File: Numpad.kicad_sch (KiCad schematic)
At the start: 196 parts, among them J1 USB_C_Receptacle_USB2.0, J2 USB_C_Receptacle_USB2.0, J3 AVR-ISP-6, Q1 DMN2041L, Q2 DMN2041L, SW1 SW_Push, SW10 SW_Push, SW11 SW_Push, SW12 SW_Push, SW13 SW_Push, SW14 SW_Push, SW15 SW_Push, SW17 SW_Push, SW18 SW_Push, SW2 SW_Push, SW20 SW_Push, SW21 SW_Push, SW23 SW_Push, SW24 SW_Push, SW25 SW_Push, SW27 SW_Push, SW28 SW_Push, SW3 SW_Push, SW30 SW_Push, SW31 SW_Push, SW32 SW_Push, SW33 SW_Push, SW34 SW_Push, SW35 SW_Push, SW36 SW_Push, SW37 SW_Push, SW38 SW_Push, SW39 SW_Push, SW4 SW_Push, SW40 SW_Push, SW41 SW_Push, SW42 SW_Push, SW43 SW_Push, SW44 SW_Push, SW45 SW_Push, SW46 SW_Push, SW47 SW_Push, SW5 SW_Push, SW6 SW_Push, SW7 SW_Push, SW8 SW_Push, SW9 SW_Push, U1 ATmega32U4-A, Y1 16MHz

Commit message: added a numpad
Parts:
- removed D10, D12, D13, D15, D22, D24, D25, D37, D4, D43, D49, D58, D66, D71, D77, D80, D81, D84, D89: D_Small, symbol Device:D_Small
- removed D11, D14, D18, D20, D26, D3, D31, D35, D39, D40, D61, D63, D67, D7, D73, D76, D79, D8, D82: LED, symbol Device:LED
- removed D?: PRTR5V0U2X, Package_TO_SOT_SMD:SOT-143, symbol Power_Protection:PRTR5V0U2X
- removed J2: USB_C_Receptacle_USB2.0, symbol Connector:USB_C_Receptacle_USB2.0
- removed R10: 1k, symbol Device:R_Small
- removed R11, R12, R13, R14, R17, R19, R25, R28, R36, R40, R42, R43, R45, R48, R50, R53, R54, R8: 470, symbol Device:R_Small
- removed R16, R26: 4.7K, symbol Device:R_Small
- removed R32, R51: 5.1k, symbol Device:R_Small
- removed SW1, SW13, SW2, SW21, SW23, SW25, SW3, SW30, SW31, SW36, SW37, SW4, SW40, SW41, SW42, SW45, SW7, SW8, SW9: SW_Push, keyswitches.pretty-2:Kailh_socket_PG1350, symbol Switch:SW_Push
- added D? (x2): D_Small, symbol Device:D_Small
- added D? (x2): LED, symbol Device:LED
- added R? (x2): 470, symbol Device:R_Small
- added SW? (x2): SW_Push, keyswitches.pretty-2:Kailh_socket_PG1350, symbol Switch:SW_Push
- R6: value 470 -> 1k
- renumbered SW28 to SW_RESET1
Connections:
- net +5V: now also D?.2 (A), D?.2 (A)
- net COL_0: now also SW?.2
- net COL_1: now also SW?.2
- net ROW_3: now also D?.1 (K)
- net ROW_4: now also D?.1 (K)
- net at D1.1 (K): now also R3.1
- net at Q1.3 (D), R1.2, R15.2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: now also R?.2, R?.2; no longer R3.2, R6.2
- net at R6.1: now also Q2.1 (G)
- net at Q2.3 (D): now also R3.2
- net CAPS_LOCK_PWM renamed NUM_LOCK_PWM
- net NUM_LOCK_PWM: now also R6.2
- net COL_5: no longer names the net of U1.36 (PF7)
- net ROW_5: no longer names the net of U1.29 (PB5)
- net ROW_6: no longer names the net of U1.30 (PB6)
- new net: D?.2 (A), SW?.1 (x2)
- new net: D?.1 (K), R?.1 (x2)
- no-connect marks 10 -> 13
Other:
- note added: "24 LEDs"
- note added: "24 switch matrix"
- note added: "NUM LOCK LED"
- note added: "NUMPAD"
- note removed: "41 LEDs"
- note removed: "41 switch matrix"
- note removed: "CAPS LOCK LED"
- note removed: "RIGHT KEEEB HALF"
- note removed: "USB-C Left HALF"
- moved on the sheet: D17, D19, D2, D21, D33, D34, D44, D46, D48, D50, D52, D56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

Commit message: numpad pcb start
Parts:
- removed D27, D28, D41, D57, D70: D_Small, symbol Device:D_Small
- removed D48, D91, D? (x2): LED, symbol Device:LED
- removed R35, R52, R? (x2): 470, symbol Device:R_Small
- removed SW10, SW11, SW14, SW17, SW33: SW_Push, keyswitches.pretty-2:Kailh_socket_PG1350, symbol Switch:SW_Push
- added D2: D_Small, Diode_SMD:D_SOD-123, symbol Device:D_Small
- added SW2: SW_Push, keyswitches.pretty-2:Kailh_socket_PG1350, symbol Switch:SW_Push
- C1, C2, C3, C4, C5, C6, C7: footprint (none) -> Capacitor_SMD:C_0402_1005Metric
- D10: renamed from D78; footprint (none) -> Diode_SMD:D_SOD-123
- D101: renamed from D83; footprint (none) -> LED_SMD:LED_PLCC_2835
- D102: renamed from D2; footprint (none) -> LED_SMD:LED_PLCC_2835
- D103: renamed from D9; footprint (none) -> LED_SMD:LED_PLCC_2835
- D104: renamed from D62; footprint (none) -> LED_SMD:LED_PLCC_2835
- D105: renamed from D74; footprint (none) -> LED_SMD:LED_PLCC_2835
- D106: renamed from D46; footprint (none) -> LED_SMD:LED_PLCC_2835
- D107: renamed from D17; footprint (none) -> LED_SMD:LED_PLCC_2835
- D108: renamed from D19; footprint (none) -> LED_SMD:LED_PLCC_2835
- D109: renamed from D56; footprint (none) -> LED_SMD:LED_PLCC_2835
- D11: renamed from D42; footprint (none) -> Diode_SMD:D_SOD-123
- D110: renamed from D44; footprint (none) -> LED_SMD:LED_PLCC_2835
- D111: renamed from D52; footprint (none) -> LED_SMD:LED_PLCC_2835
- D112: renamed from D88; footprint (none) -> LED_SMD:LED_PLCC_2835
- D113: renamed from D33; footprint (none) -> LED_SMD:LED_PLCC_2835
- D114: renamed from D75; footprint (none) -> LED_SMD:LED_PLCC_2835
- D115: renamed from D34; footprint (none) -> LED_SMD:LED_PLCC_2835
- D116: renamed from D72; footprint (none) -> LED_SMD:LED_PLCC_2835
- D117: renamed from D50; footprint (none) -> LED_SMD:LED_PLCC_2835
- D118: renamed from D64; footprint (none) -> LED_SMD:LED_PLCC_2835
- D119: renamed from D85; footprint (none) -> LED_SMD:LED_PLCC_2835
- D12: renamed from D87; footprint (none) -> Diode_SMD:D_SOD-123
- D120: renamed from D86; footprint (none) -> LED_SMD:LED_PLCC_2835
- D125: renamed from D1; footprint (none) -> LED_SMD:LED_PLCC_2835
- D13: renamed from D30; footprint (none) -> Diode_SMD:D_SOD-123
- D14: renamed from D16; footprint (none) -> Diode_SMD:D_SOD-123
- D15: renamed from D5; footprint (none) -> Diode_SMD:D_SOD-123
- D16: renamed from D51; footprint (none) -> Diode_SMD:D_SOD-123
- D17: renamed from D47; footprint (none) -> Diode_SMD:D_SOD-123
- D18: renamed from D6; footprint (none) -> Diode_SMD:D_SOD-123
- D19: renamed from D29; footprint (none) -> Diode_SMD:D_SOD-123
- D20: renamed from D45; footprint (none) -> Diode_SMD:D_SOD-123
- D21: renamed from D68; footprint (none) -> Diode_SMD:D_SOD-123
- D3, D7: renamed from D?; footprint (none) -> Diode_SMD:D_SOD-123
- D4: renamed from D60; footprint (none) -> Diode_SMD:D_SOD-123
- D5: renamed from D54; footprint (none) -> Diode_SMD:D_SOD-123
- D6: renamed from D23; footprint (none) -> Diode_SMD:D_SOD-123
- D8: renamed from D69; footprint (none) -> Diode_SMD:D_SOD-123
- D9: renamed from D90; footprint (none) -> Diode_SMD:D_SOD-123
- F1: footprint (none) -> Keebio-Parts:Fuse_0805
- J1: footprint (none) -> Connector_USB:USB_C_Receptacle_HRO_TYPE-C-31-M-12
- J3: footprint (none) -> Keebio-Parts:ICSP_1.27mm
- R101: renamed from R30; footprint (none) -> Resistor_SMD:R_0402_1005Metric
- R102: renamed from R39; footprint (none) -> Resistor_SMD:R_0402_1005Metric
- R103: renamed from R5; footprint (none) -> Resistor_SMD:R_0402_1005Metric
- R104: renamed from R1; footprint (none) -> Resistor_SMD:R_0402_1005Metric
- R105: renamed from R37; footprint (none) -> Resistor_SMD:R_0402_1005Metric
- R106: renamed from R46; footprint (none) -> Resistor_SMD:R_0402_1005Metric
- R107: renamed from R47; footprint (none) -> Resistor_SMD:R_0402_1005Metric
- R108: renamed from R18; footprint (none) -> Resistor_SMD:R_0402_1005Metric
- R109: renamed from R49; footprint (none) -> Resistor_SMD:R_0402_1005Metric
- R110: renamed from R7; footprint (none) -> Resistor_SMD:R_0402_1005Metric
- R111: renamed from R24; footprint (none) -> Resistor_SMD:R_0402_1005Metric
- R112: renamed from R33; footprint (none) -> Resistor_SMD:R_0402_1005Metric
- R113: renamed from R38; footprint (none) -> Resistor_SMD:R_0402_1005Metric
- R114: renamed from R29; footprint (none) -> Resistor_SMD:R_0402_1005Metric
- R115: renamed from R9; footprint (none) -> Resistor_SMD:R_0402_1005Metric
- R116: renamed from R20; footprint (none) -> Resistor_SMD:R_0402_1005Metric
- R117: renamed from R27; footprint (none) -> Resistor_SMD:R_0402_1005Metric
- R118: renamed from R15; footprint (none) -> Resistor_SMD:R_0402_1005Metric
- R119: renamed from R4; footprint (none) -> Resistor_SMD:R_0402_1005Metric
- R120: renamed from R41; footprint (none) -> Resistor_SMD:R_0402_1005Metric
- R121: renamed from R21; footprint (none) -> Resistor_SMD:R_0402_1005Metric
- R2, R22, R23, R3, R31, R34, R44, R6: footprint (none) -> Resistor_SMD:R_0402_1005Metric
- U1: footprint ATmega32U4:ATmega32U4 -> Package_QFP:TQFP-44_10x10mm_P0.8mm
- Y1: footprint (none) -> Crystal:Crystal_SMD_3225-4Pin_3.2x2.5mm
- gave numbers to parts that had none: 2
- renumbered D21 to D1, Q1 to Q101, SW39 to SW10, SW44 to SW11, SW5 to SW12, SW47 to SW13, SW20 to SW14, SW18 to SW15, SW27 to SW16, SW32 to SW17, SW24 to SW18, SW12 to SW19, SW38 to SW20, SW35 to SW21, SW34 to SW4, SW6 to SW5, SW15 to SW6, SW43 to SW8, SW46 to SW9
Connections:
- net COL_0: now also SW2.2
- net ROW_4: now also D2.1 (K)
- net COL_4: no longer names the net of U1.37 (PF6)
- new net: D2.2 (A), SW2.1
- no-connect marks 13 -> 14
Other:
- note added: "20 LEDs"
- note added: "20 SWITCH MATRIX"
- note removed: "24 LEDs"
- note removed: "24 switch matrix"
- moved on the sheet: Q101, R121

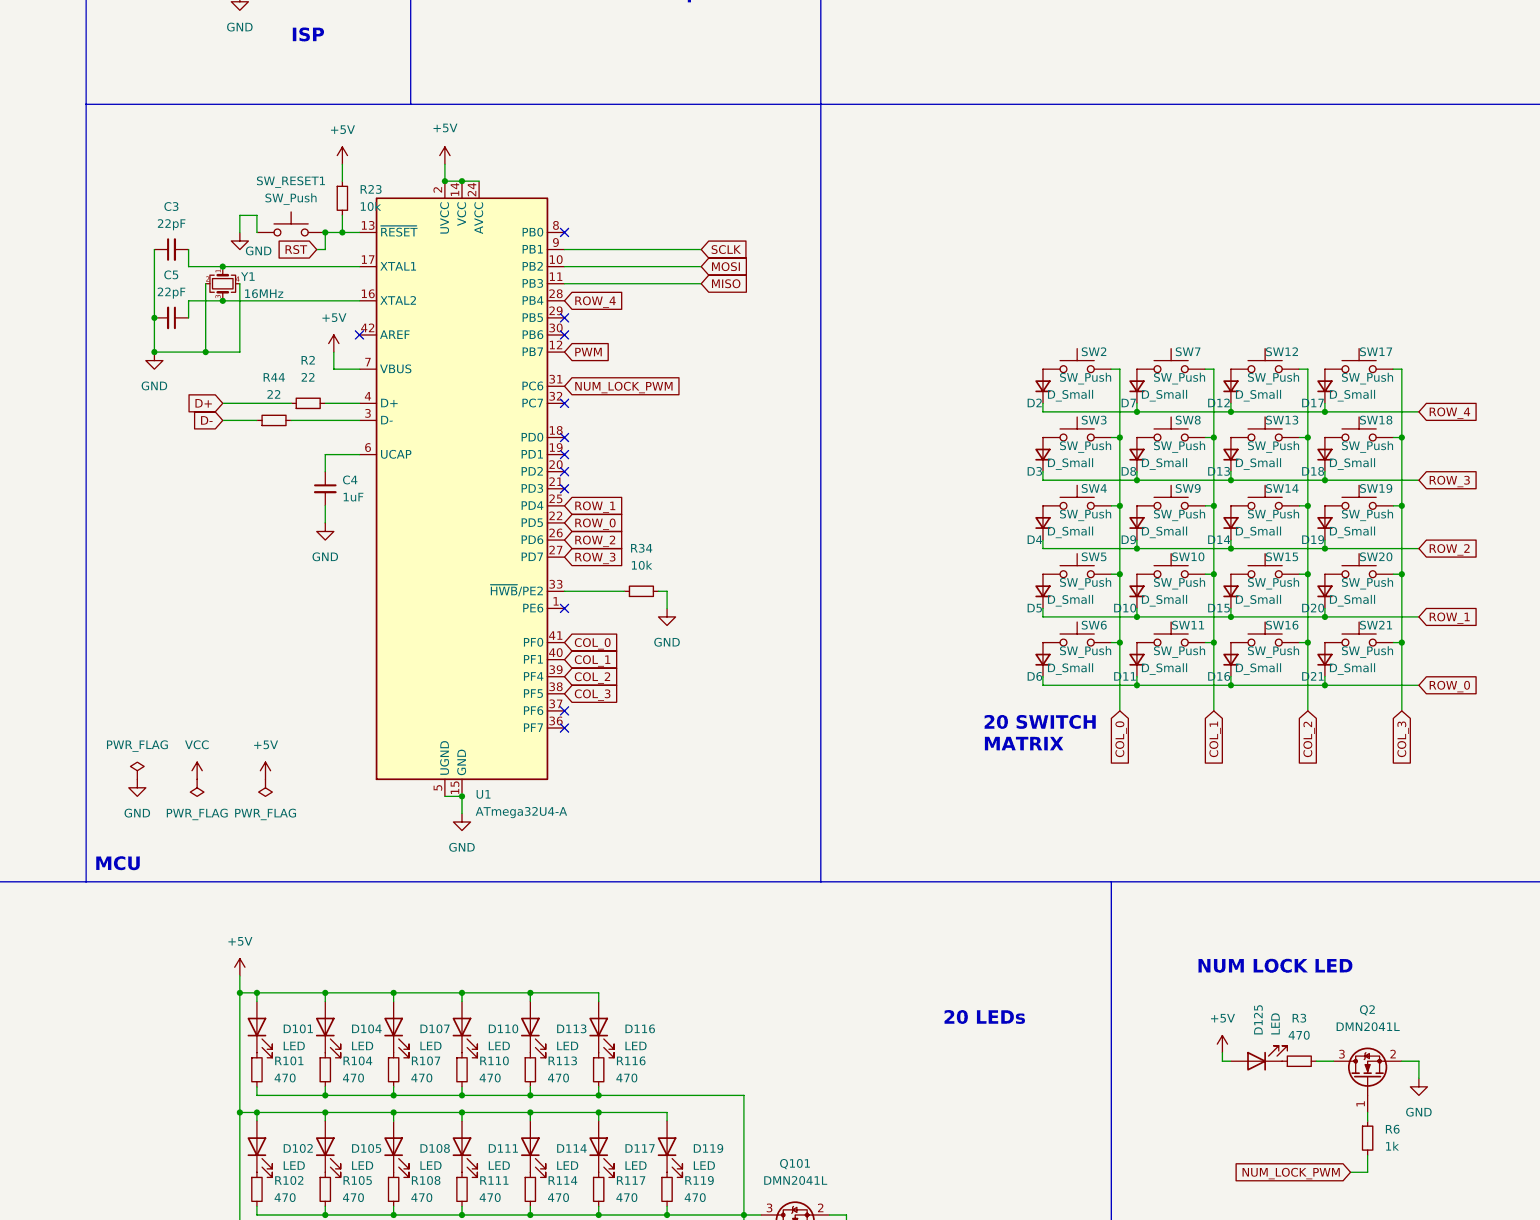
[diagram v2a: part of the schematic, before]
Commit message: switched atmega32u4 to u2 for the smaller footprint
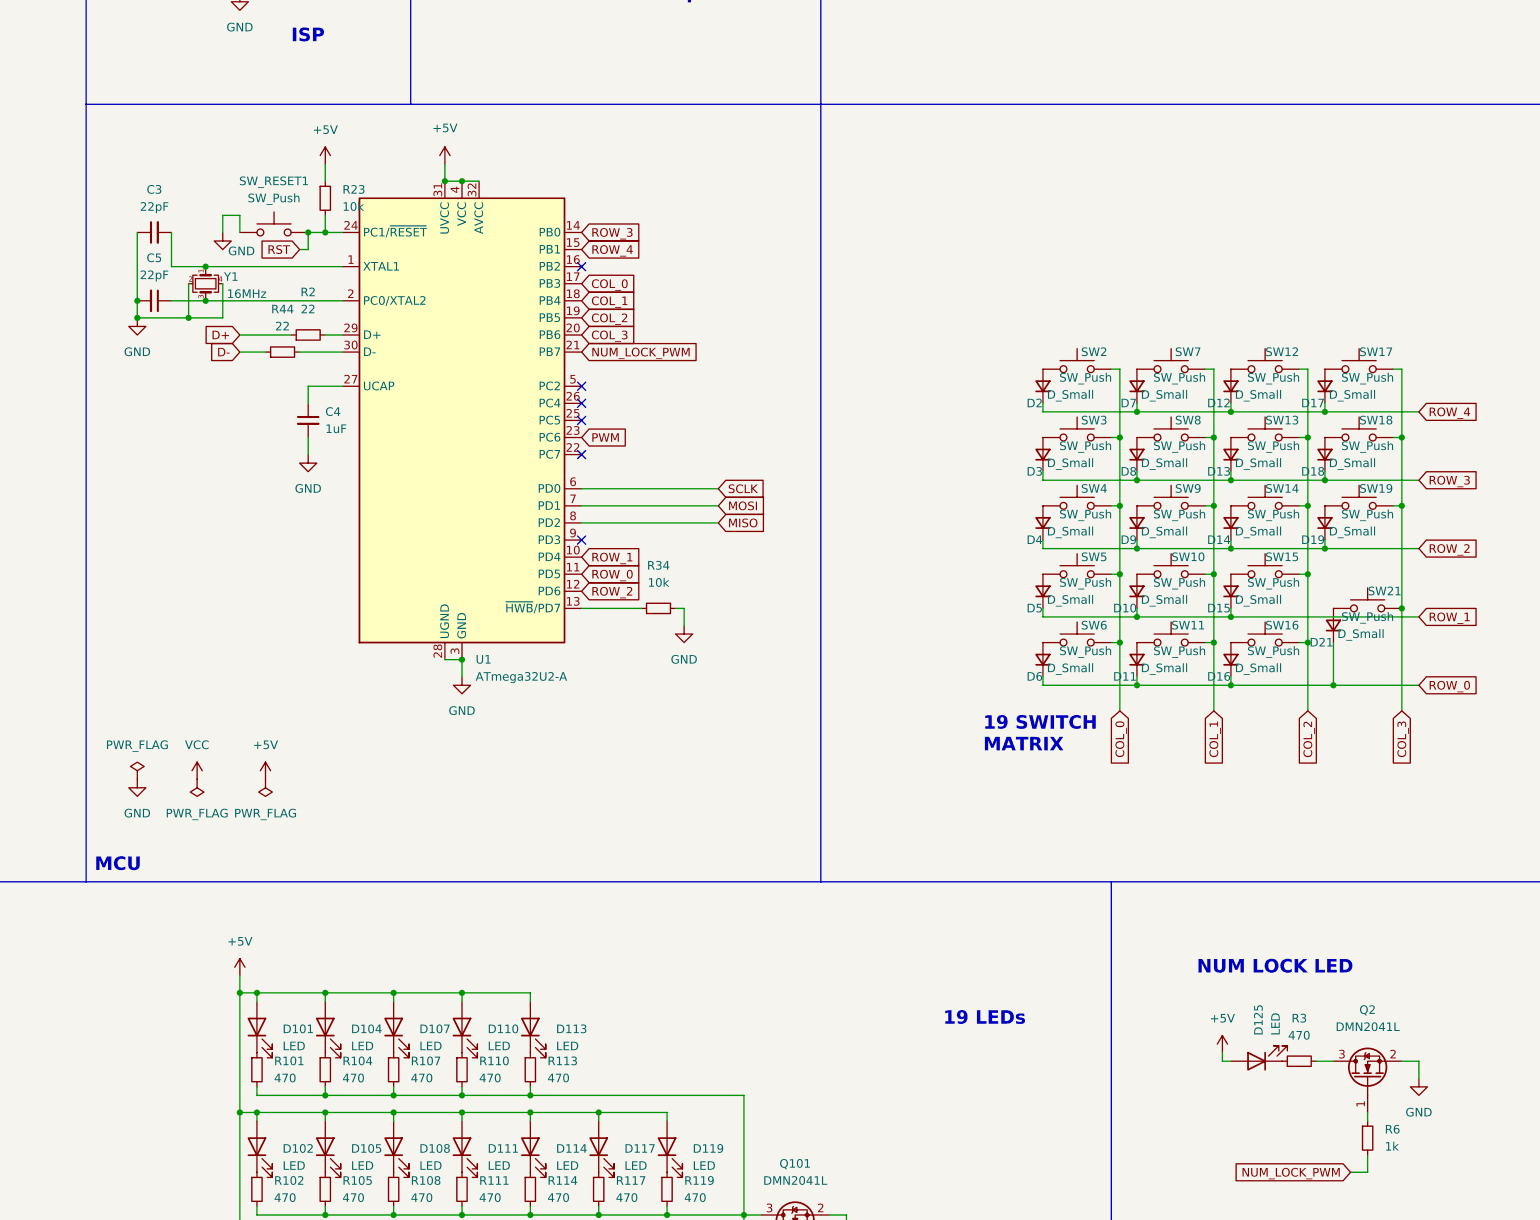
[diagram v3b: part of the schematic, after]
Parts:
- removed D116: LED, LED_SMD:LED_PLCC_2835, symbol Device:LED
- removed D20: D_Small, Diode_SMD:D_SOD-123, symbol Device:D_Small
- removed R116: 470, Resistor_SMD:R_0402_1005Metric, symbol Device:R_Small
- removed SW20: SW_Push, keyswitches.pretty-2:Kailh_socket_PG1350, symbol Switch:SW_Push
- removed U1: ATmega32U4-A, Package_QFP:TQFP-44_10x10mm_P0.8mm, symbol MCU_Microchip_ATmega:ATmega32U4-A
- added U1: ATmega32U2-A, Package_QFP:TQFP-32_7x7mm_P0.8mm, symbol MCU_Microchip_ATmega:ATmega32U2-A
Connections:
- net +5V: now also U1.31 (UVCC), U1.32 (AVCC), U1.4 (VCC)
- net COL_0: now also U1.17 (PB3)
- net COL_1: now also U1.18 (PB4)
- net COL_2: now also U1.19 (PB5)
- net COL_3: now also U1.20 (PB6)
- net GND: now also U1.28 (UGND), U1.3 (GND)
- net MISO: now also U1.8 (PD2)
- net MOSI: now also U1.7 (PD1)
- net NUM_LOCK_PWM: now also U1.21 (PB7)
- net PWM: now also U1.23 (PC6)
- net ROW_0: now also U1.11 (PD5)
- net ROW_1: now also U1.10 (PD4)
- net ROW_2: now also U1.12 (PD6)
- net ROW_3: now also U1.14 (PB0)
- net ROW_4: now also U1.15 (PB1)
- net RST: now also U1.24 (PC1/~{RESET})
- net SCLK: now also U1.6 (PD0)
- net at C5.1, Y1.3: now also U1.2 (PC0/XTAL2)
- net at C3.2, Y1.1: now also U1.1 (XTAL1)
- net at R44.2: now also U1.30 (D-)
- net at R34.1: now also U1.13 (~{HWB}/PD7)
- net at R2.2: now also U1.29 (D+)
- net at C4.1: now also U1.27 (UCAP)
- no-connect marks 14 -> 8
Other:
- note added: "19 LEDs"
- note added: "19 SWITCH MATRIX"
- note removed: "20 LEDs"
- note removed: "20 SWITCH MATRIX"
- moved on the sheet: C3, C4, C5, D21, R2, R23, R34, R44, SW21, SW_RESET1, Y1
